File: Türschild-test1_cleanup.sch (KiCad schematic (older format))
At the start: 91 parts, among them J1 Conn_01x03_Male, J2 Conn_01x03_Female, J3 USB_B_Micro, J4 Conn_01x24_MountingPin, Q3 Si1442DH, U1 BQ25570, U2 BQ27441-G1, U3 ESP32-WROOM-32, U4 CP2102N-A01-GQFN28, U5 LM1117-3.3

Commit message: HowTo Changes mit Daniel
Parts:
- removed D7, D8, D9: D_Schottky_Small, Diode_SMD:D_0603_1608Metric_Castellated, symbol Device:D_Schottky_Small
- removed Q3: Si1442DH, Package_TO_SOT_SMD:SOT-363_SC-70-6, symbol Transistor_FET:Si1442DH
- added C25: 100n, Capacitor_SMD:C_0603_1608Metric_Pad1.05x0.95mm_HandSolder, symbol Device:C
- added C26: 4u7, Capacitor_SMD:C_0805_2012Metric_Pad1.15x1.40mm_HandSolder, symbol Device:C
- added Q1: IRLML2502PbF, Package_TO_SOT_SMD:SOT-23, symbol Tuerschld:IRLML2502PbF
- added R22: 1K, Resistor_SMD:R_0603_1608Metric_Pad1.05x0.95mm_HandSolder, symbol Device:R
- added R23: 4K7, Resistor_SMD:R_0603_1608Metric_Pad1.05x0.95mm_HandSolder, symbol Device:R
- added U6: WE-TVS-82400152, Package_TO_SOT_SMD:SOT-563, symbol Power_Protection:WE-TVS-82400152
- C1, C10, C11, C2: footprint Capacitor_SMD:C_0603_1608Metric -> Capacitor_SMD:C_0805_2012Metric_Pad1.15x1.40mm_HandSolder
- C12, C24: footprint (none) -> Capacitor_SMD:C_0603_1608Metric_Pad1.05x0.95mm_HandSolder
- C13, C14, C15, C16, C17, C18, C19, C20, C21, C22, C5, C6, C7, C8, C9: footprint Capacitor_SMD:C_0603_1608Metric -> Capacitor_SMD:C_0603_1608Metric_Pad1.05x0.95mm_HandSolder
- C3, C4: value 0,1µF -> 100n; footprint Capacitor_SMD:C_0603_1608Metric -> Capacitor_SMD:C_0603_1608Metric_Pad1.05x0.95mm_HandSolder
- D1, D2, D3, D4: footprint LED_SMD:LED_0603_1608Metric_Castellated -> LED_SMD:LED_0603_1608Metric_Pad1.05x0.95mm_HandSolder
- D10, D11, D12: value MBR0530 -> MBR0530T1G
- D5, D6: value D_Schottky_Small -> SS16; footprint Diode_SMD:D_0603_1608Metric_Castellated -> Diode_SMD:D_SMA-SMB_Universal_Handsoldering
- J1: footprint Connector_Molex:Molex_Micro-Latch_53253-0370_1x03_P2.00mm_Vertical -> Connector_PinHeader_2.00mm:PinHeader_1x03_P2.00mm_Vertical_SMD_Pin1Left
- J2: footprint Connector_Molex:Molex_Micro-Latch_53253-0370_1x03_P2.00mm_Vertical -> Connector_PinSocket_2.00mm:PinSocket_1x03_P2.00mm_Vertical_SMD_Pin1Right
- J3: footprint Connector_USB:USB_Micro-B_Wuerth_614105150721_Vertical_CircularHoles -> Connector_USB:USB_Mini-B_Wuerth_65100516121_Horizontal
- J4: footprint Connector_FFC-FPC:Hirose_FH12-24S-0.5SH_1x24-1MP_P0.50mm_Horizontal -> Connector_FFC-FPC:Molex_502244-2430_1x24-1MP_P0.5mm_Horizontal
- L1: footprint Inductor_SMD:L_0603_1608Metric -> Inductor_SMD:L_Wuerth_WE-TPC-3816; WE (none) -> 744031220
- L2, L3: footprint Inductor_SMD:L_0603_1608Metric -> Inductor_SMD:L_Wuerth_WE-TPC-3816
- R1, R10, R11, R12, R13, R14, R15, R16, R17, R18, R19, R2, R20, R24, R26, R3, R4, R5, R6, R7, R8, R9, Rok1, Rok2, Rok3, Rout1, Rout2, Rov1, Rov2: footprint Resistor_SMD:R_0603_1608Metric -> Resistor_SMD:R_0603_1608Metric_Pad1.05x0.95mm_HandSolder
- R21: footprint (none) -> Resistor_SMD:R_0603_1608Metric_Pad1.05x0.95mm_HandSolder
- SC1: footprint (none) -> Connector_PinHeader_2.54mm:PinHeader_1x02_P2.54mm_Horizontal
- U5: footprint (none) -> Package_TO_SOT_SMD:SOT-223-3_TabPin2
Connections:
- net labels added: USBID
- wire segments 344 -> 365
- no-connect marks 0 -> 3
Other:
- moved on the sheet: C1, C10, C11, C12, C13, C14, C15, C16, C17, C18, C19, C2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

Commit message: Version 1
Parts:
- Q1: symbol Tuerschld:IRLML2502PbF -> Türschild-test1_cleanup-rescue:IRLML2502PbF-Tuerschld
- U3: symbol RF_Module:ESP32-WROOM-32 -> Türschild-test1_cleanup-rescue:ESP32-WROOM-32-RF_Module
- U6: symbol Power_Protection:WE-TVS-82400152 -> Türschild-test1_cleanup-rescue:WE-TVS-82400152-Power_Protection
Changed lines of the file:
@@
 EESchema Schematic File Version 4
 LIBS:Türschild-test1_cleanup-cache
-EELAYER 26 0
+EELAYER 30 0
 EELAYER END
 $Descr A3 16535 11693
@@
 	3800 10050 4000 10050
 $Comp
-L RF_Module:ESP32-WROOM-32 U3
+L Türschild-test1_cleanup-rescue:ESP32-WROOM-32-RF_Module U3
 U 1 1 5E6AA9AA
 P 3200 9250
@@
 Wire Wire Line
 	7925 4600 7975 4600
-$Comp
-L power:GND #PWR0106
-U 1 1 5E3D7284
-P 7850 4350
-F 0 "#PWR0106" H 7850 4100 50  0001 C CNN
-F 1 "GND" H 7950 4400 50  0000 R CNN
-F 2 "" H 7850 4350 50  0001 C CNN
-F 3 "" H 7850 4350 50  0001 C CNN
-	1    7850 4350
-	1    0    0    -1
-$EndComp
 Wire Wire Line
 	7975 4750 7975 4600
@@
 $EndComp
 $Comp
-L Tuerschld:IRLML2502PbF Q1
+L Türschild-test1_cleanup-rescue:IRLML2502PbF-Tuerschld Q1
 U 1 1 5EA0F170
 P 8325 7225
@@
 	3650 3100 3875 3100
 Connection ~ 3650 3100
+Wire Wire Line
+	2175 3100 1450 3100
+Wire Wire Line
+	1450 3100 1450 3150
+Connection ~ 2175 3100
+Wire Wire Line
+	2425 3100 2375 3100
+Wire Wire Line
+	2375 3100 2375 3600
+Wire Wire Line
+	2375 3600 2425 3600
+Wire Wire Line
+	2725 3100 2925 3100
+Connection ~ 2925 3100
+Wire Wire Line
+	1450 3450 1450 3525
+Connection ~ 1450 3525
+$Comp
+L Türschild-test1_cleanup-rescue:WE-TVS-82400152-Power_Protection U6
+U 1 1 5EF0B64C
+P 1850 4000
+F 0 "U6" H 1825 4275 50  0000 C CNN
+F 1 "WE-TVS-82400152" H 1925 4350 50  0000 C CNN
+F 2 "Package_TO_SOT_SMD:SOT-563" H 1850 4250 50  0001 C CNN
+F 3 "https://www.we-online.de/katalog/datasheet/82400152.pdf" H 1850 4250 50  0001 C CNN
+	1    1850 4000
+	1    0    0    1
+$EndComp
+Wire Wire Line
+	1300 3700 1450 3700
+Wire Wire Line
+	1000 5900 1650 5900
+Wire Wire Line
+	1650 5900 2925 5900
+Wire Wire Line
+	2825 2875 2825 3200
+Wire Wire Line
+	2400 2350 2400 2875
+Wire Wire Line
+	2400 2875 2825 2875
+Wire Wire Line
+	1375 4000 1300 4000
+$Comp
+L power:GND #PWR0109
+U 1 1 5F12DC1E
+P 1450 4300
+F 0 "#PWR0109" H 1450 4050 50  0001 C CNN
+F 1 "GND" H 1455 4127 50  0000 C CNN
+F 2 "" H 1450 4300 50  0001 C CNN
+F 3 "" H 1450 4300 50  0001 C CNN
+	1    1450 4300
+	1    0    0    -1
+$EndComp
+Wire Wire Line
+	1450 4000 1500 4000
+Wire Wire Line
+	1725 3225 1725 3300
+Wire Wire Line
+	2075 3225 2175 3225
+Wire Wire Line
+	1450 3525 2250 3525
+Wire Wire Line
+	2250 3525 2250 4000
+Wire Wire Line
+	2250 4000 2200 4000
+Wire Wire Line
+	1450 4000 1450 4300
+Wire Wire Line
+	2200 3900 2425 3900
+Wire Wire Line
+	2425 4000 2300 4000
+Wire Wire Line
+	2300 4000 2300 4100
+Wire Wire Line
+	2300 4100 2200 4100
+Wire Wire Line
+	1375 4100 1375 4000
+Wire Wire Line
+	1500 4100 1375 4100
+Wire Wire Line
+	1500 3900 1300 3900
+$Comp
+L Device:R R23
+U 1 1 5F3B548A
+P 1325 4550
+F 0 "R23" H 1375 4600 50  0000 L CNN
+F 1 "4K7" H 1375 4500 50  0000 L CNN
+F 2 "Resistor_SMD:R_0603_1608Metric_Pad1.05x0.95mm_HandSolder" V 1255 4550 50  0001 C CNN
+F 3 "~" H 1325 4550 50  0001 C CNN
+	1    1325 4550
+	-1   0    0    1
+$EndComp
+Wire Wire Line
+	1325 4100 1325 4400
+Wire Wire Line
+	1400 4800 1325 4800
+Wire Wire Line
+	1325 4800 1325 4700
 $Comp
 L Device:R R22
@@
 	0    1    1    0
 $EndComp
-Wire Wire Line
-	2175 3100 1450 3100
-Wire Wire Line
-	1450 3100 1450 3150
-Connection ~ 2175 3100
-Wire Wire Line
-	2425 3100 2375 3100
-Wire Wire Line
-	2375 3100 2375 3600
-Wire Wire Line
-	2375 3600 2425 3600
-Wire Wire Line
-	2725 3100 2925 3100
-Connection ~ 2925 3100
-Wire Wire Line
-	1450 3450 1450 3525
-Connection ~ 1450 3525
-$Comp
-L Power_Protection:WE-TVS-82400152 U6
-U 1 1 5EF0B64C
-P 1850 4000
-F 0 "U6" H 1825 4275 50  0000 C CNN
-F 1 "WE-TVS-82400152" H 1925 4350 50  0000 C CNN
-F 2 "Package_TO_SOT_SMD:SOT-563" H 1850 4250 50  0001 C CNN
-F 3 "https://www.we-online.de/katalog/datasheet/82400152.pdf" H 1850 4250 50  0001 C CNN
-	1    1850 4000
-	1    0    0    1
-$EndComp
-Wire Wire Line
-	1300 3700 1450 3700
-Wire Wire Line
-	1000 5900 1650 5900
-Wire Wire Line
-	1650 5900 2925 5900
-Wire Wire Line
-	2825 2875 2825 3200
-Wire Wire Line
-	2400 2350 2400 2875
-Wire Wire Line
-	2400 2875 2825 2875
-Wire Wire Line
-	1375 4000 1300 4000
-$Comp
-L power:GND #PWR0109
-U 1 1 5F12DC1E
-P 1450 4300
-F 0 "#PWR0109" H 1450 4050 50  0001 C CNN
-F 1 "GND" H 1455 4127 50  0000 C CNN
-F 2 "" H 1450 4300 50  0001 C CNN
-F 3 "" H 1450 4300 50  0001 C CNN
-	1    1450 4300
-	1    0    0    -1
-$EndComp
-Wire Wire Line
-	1450 4000 1500 4000
-Wire Wire Line
-	1725 3225 1725 3300
-Wire Wire Line
-	2075 3225 2175 3225
-Wire Wire Line
-	1450 3525 2250 3525
-Wire Wire Line
-	2250 3525 2250 4000
-Wire Wire Line
-	2250 4000 2200 4000
-Wire Wire Line
-	1450 4000 1450 4300
-Wire Wire Line
-	2200 3900 2425 3900
-Wire Wire Line
-	2425 4000 2300 4000
-Wire Wire Line
-	2300 4000 2300 4100
-Wire Wire Line
-	2300 4100 2200 4100
-Wire Wire Line
-	1375 4100 1375 4000
-Wire Wire Line
-	1500 4100 1375 4100
-Wire Wire Line
-	1500 3900 1300 3900
-$Comp
-L Device:R R23
-U 1 1 5F3B548A
-P 1325 4550
-F 0 "R23" H 1375 4600 50  0000 L CNN
-F 1 "4K7" H 1375 4500 50  0000 L CNN
-F 2 "Resistor_SMD:R_0603_1608Metric_Pad1.05x0.95mm_HandSolder" V 1255 4550 50  0001 C CNN
-F 3 "~" H 1325 4550 50  0001 C CNN
-	1    1325 4550
-	-1   0    0    1
-$EndComp
-Wire Wire Line
-	1325 4100 1325 4400
-Wire Wire Line
-	1400 4800 1325 4800
-Wire Wire Line
-	1325 4800 1325 4700
+$Comp
+L power:GND #PWR0106
+U 1 1 5E3D7284
+P 7850 4350
+F 0 "#PWR0106" H 7850 4100 50  0001 C CNN
+F 1 "GND" H 7950 4400 50  0000 R CNN
+F 2 "" H 7850 4350 50  0001 C CNN
+F 3 "" H 7850 4350 50  0001 C CNN
+	1    7850 4350
+	1    0    0    -1
+$EndComp
 $EndSCHEMATC

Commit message: layout verbessert
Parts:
- added C?: 100n, Capacitor_SMD:C_0603_1608Metric_Pad1.05x0.95mm_HandSolder, symbol Device:C
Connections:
- net GND: now also C?.2
- net at R7.2, U1.18 (VBAT), U2.7 (SRN): now also C?.1
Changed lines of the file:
@@
 	1    0    0    -1
 $EndComp
+$Comp
+L Device:C C?
+U 1 1 5EBD1462
+P 6300 3050
+F 0 "C?" H 6300 3200 50  0000 L CNN
+F 1 "100n" H 6300 2950 50  0000 L CNN
+F 2 "Capacitor_SMD:C_0603_1608Metric_Pad1.05x0.95mm_HandSolder" H 6338 2900 50  0001 C CNN
+F 3 "~" H 6300 3050 50  0001 C CNN
+	1    6300 3050
+	1    0    0    -1
+$EndComp
+$Comp
+L power:GND #PWR?
+U 1 1 5EBD2783
+P 6300 3300
+F 0 "#PWR?" H 6300 3050 50  0001 C CNN
+F 1 "GND" H 6450 3250 50  0000 C CNN
+F 2 "" H 6300 3300 50  0001 C CNN
+F 3 "" H 6300 3300 50  0001 C CNN
+	1    6300 3300
+	1    0    0    -1
+$EndComp
+Wire Wire Line
+	6300 3300 6300 3200
+Wire Wire Line
+	6300 2900 6300 2700
+Wire Wire Line
+	6300 2700 6125 2700
+Connection ~ 6125 2700
 $EndSCHEMATC

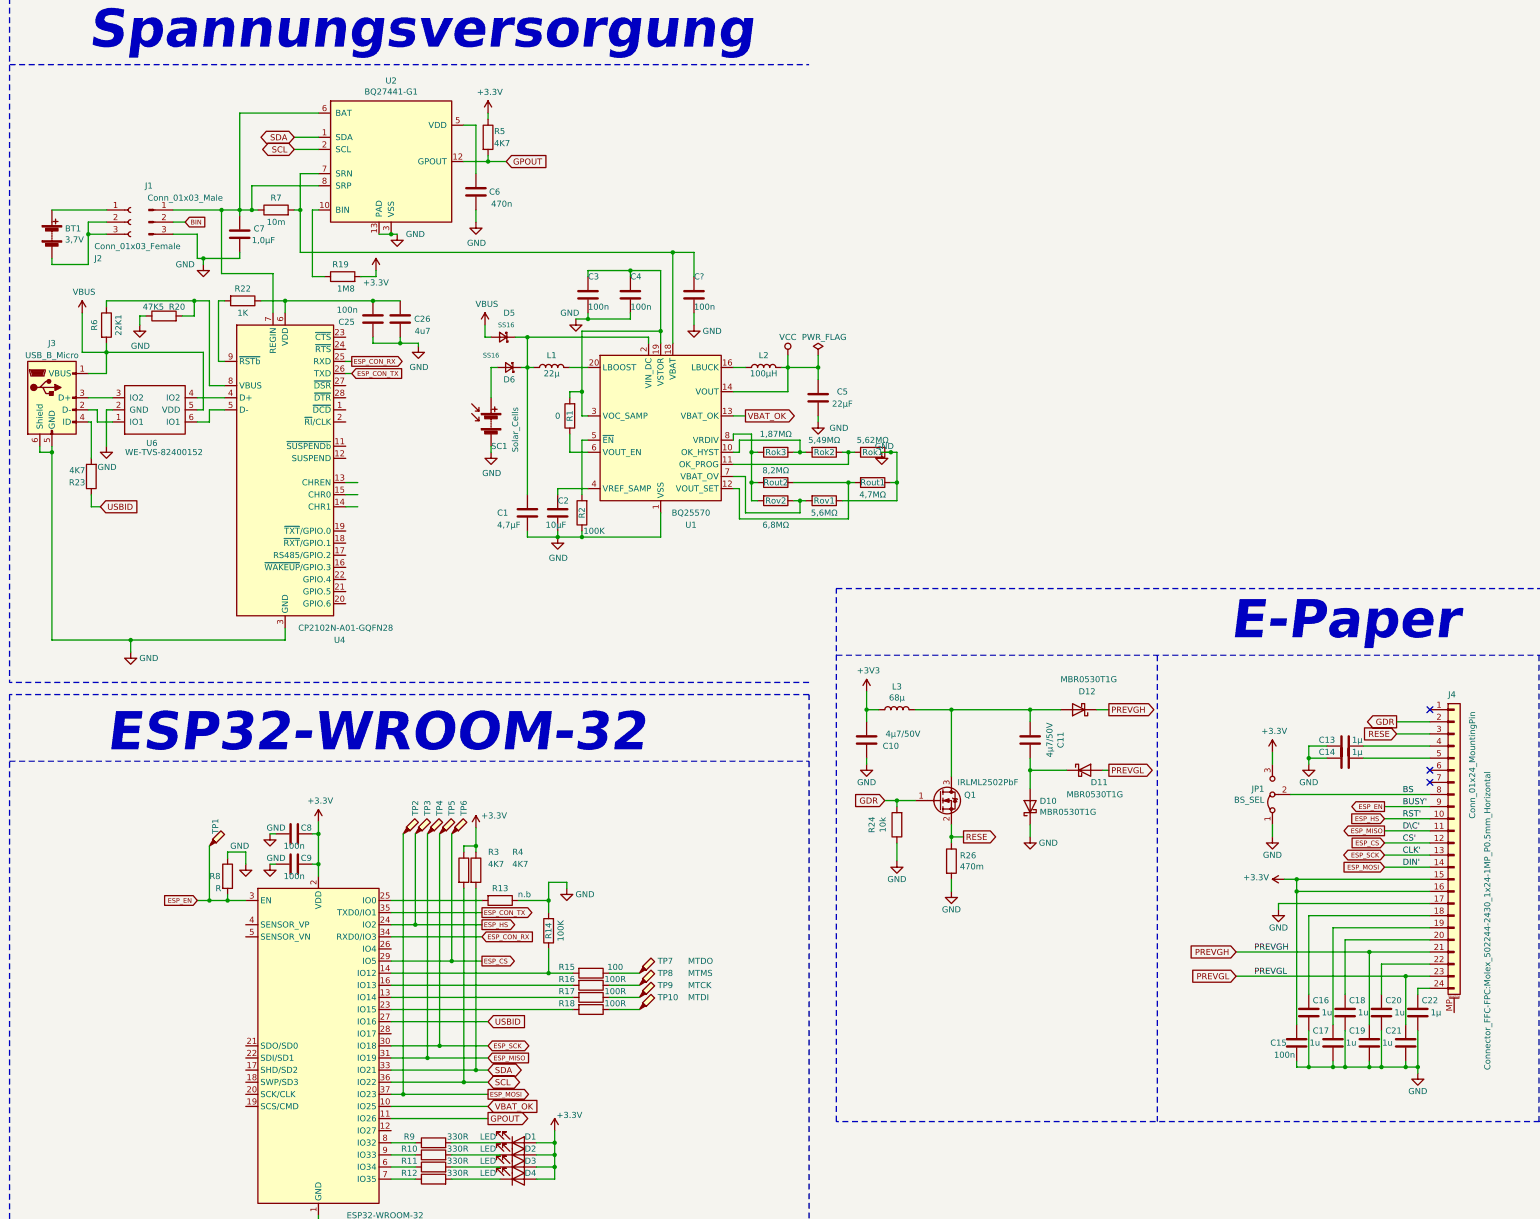
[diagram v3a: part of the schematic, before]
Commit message: Akkustecker hinzugefügt layout verbessert
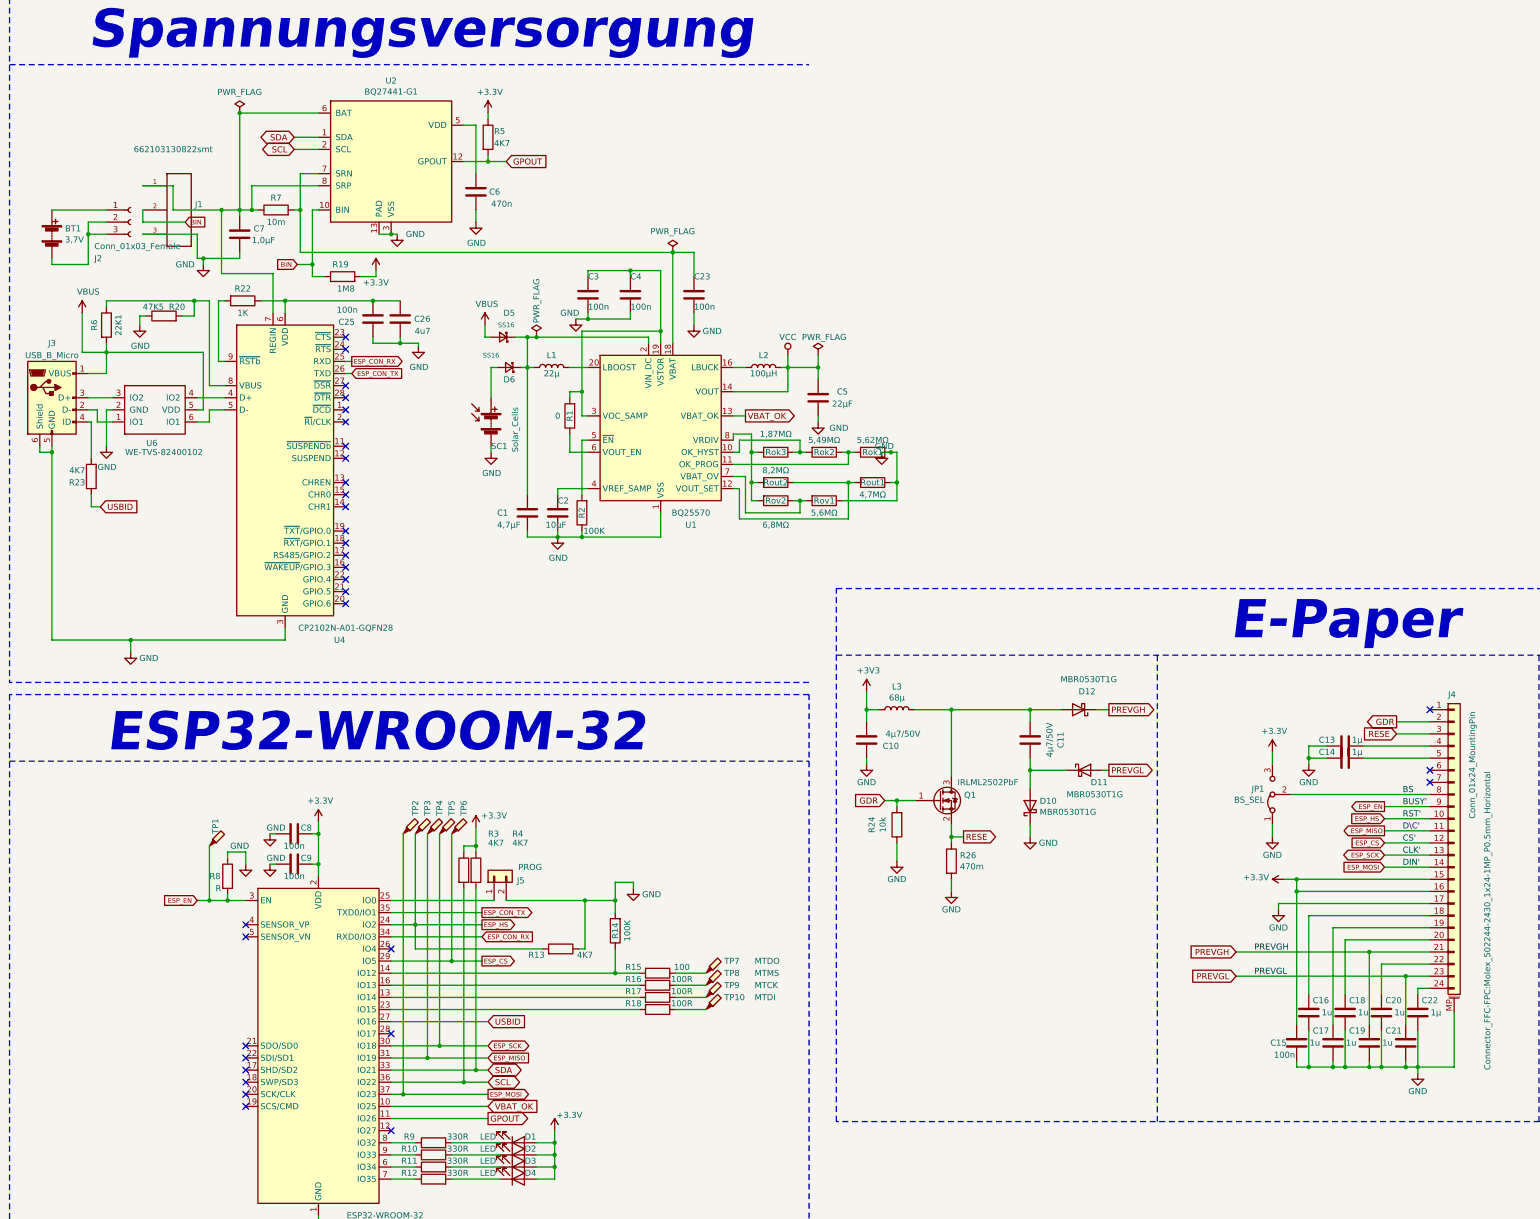
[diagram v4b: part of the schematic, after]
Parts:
- removed J1: Conn_01x03_Male, Connector_PinHeader_2.00mm:PinHeader_1x03_P2.00mm_Vertical_SMD_Pin1Left, symbol Connector:Conn_01x03_Male
- added J1: 662103130822smt, Tuerschild-Kiacad:662103130822, symbol Türschild-test1_cleanup-rescue:662103130822smt
- added J5: PROG, Jumper:SolderJumper-2_P1.3mm_Bridged_Pad1.0x1.5mm, symbol Connector_Generic:Conn_01x02
- R13: value n.b -> 4K7
- U6: value WE-TVS-82400152 -> WE-TVS-82400102; footprint Package_TO_SOT_SMD:SOT-563 -> Package_TO_SOT_SMD:SOT-23-6_Handsoldering
- gave numbers to parts that had none: 1
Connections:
- net BIN: now also R19.1, U2.10 (BIN), J1.2
- net ESP_HS: now also R13.2
- net GND: now also J4.MP (MountPin), J1.3, J5.2 (Pin_2)
- net at C7.1, R7.1, U2.6 (BAT)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: now also J1.1
- net at U3.25 (IO0): now also J5.1 (Pin_1); no longer R13.2
- no-connect marks 3 -> 32
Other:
- moved on the sheet: R14, R15, R16, R17, R18, TP10, TP7, TP8, TP9

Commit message: Update 22.10.20
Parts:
- added J6: Conn_01x08_Female, Connector_PinHeader_1.00mm:PinHeader_1x08_P1.00mm_Horizontal, symbol Connector:Conn_01x08_Female
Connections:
- net +3V3: now also J6.8 (Pin_8)
- net ESP_CS: now also J6.4 (Pin_4)
- net ESP_EN: now also J6.1 (Pin_1)
- net ESP_HS: now also J6.2 (Pin_2)
- net ESP_MISO: now also J6.3 (Pin_3)
- net ESP_MOSI: now also J6.6 (Pin_6)
- net ESP_SCK: now also J6.5 (Pin_5)
- net GND: now also J6.7 (Pin_7)
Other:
- moved on the sheet: C10, C11, C12, C13, C14, C15, C16, C17, C18, C19, C20, C21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
